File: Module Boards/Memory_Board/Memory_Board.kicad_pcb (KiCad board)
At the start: 6 copper layers, 10.8 x 15.2 mm, 17 parts, among them U1 MX25U12832FZNI02-TR, U2 MX25U25643GZ4I00-T

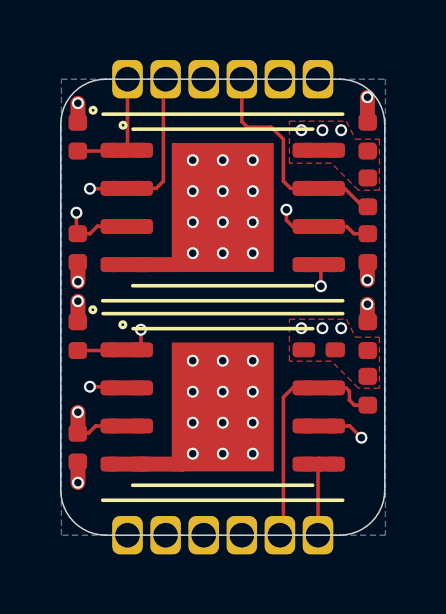
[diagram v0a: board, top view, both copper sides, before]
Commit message: Added Memory Socket Board. Improved layout of the Module Board
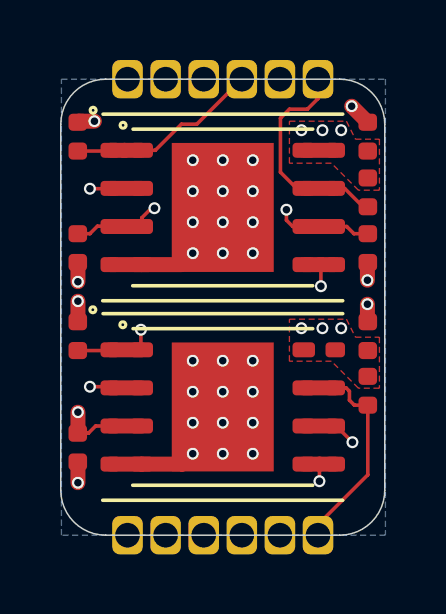
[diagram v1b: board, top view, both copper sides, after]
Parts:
- turned J1 to 90 degrees
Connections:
- J1 pad 10: ~{FLASH_1_WP}_(IO2) -> GND
- J1 pad 12: ~{FLASH_1_CS} -> FLASH_MOSI_(IO0)
- J1 pad 3: ~{FLASH_2_WP}_(IO2) -> FLASH_CLK
- J1 pad 5: ~{FLASH_2_RST}_(IO3) -> ~{FLASH_2_WP}_(IO2)
- J1 pad 6: FLASH_MOSI_(IO0) -> ~{FLASH_2_RST}_(IO3)
- J1 pad 7: FLASH_CLK -> ~{FLASH_1_RST}_(IO3)
- J1 pad 8: GND -> ~{FLASH_1_WP}_(IO2)
- J1 pad 9: ~{FLASH_1_RST}_(IO3) -> ~{FLASH_1_CS}
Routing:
- net ~{FLASH_2_WP}_(IO2): track 9.23 -> 18.8 mm
- net FLASH_MOSI_(IO0): track 15.3 -> 22.9 mm, vias 1 -> 2
- net ~{FLASH_1_CS}: track 4.56 -> 6.46 mm
- net FLASH_CLK: track 22.3 -> 24.1 mm
- net ~{FLASH_2_CS}: track 11.7 -> 12.2 mm
- net ~{FLASH_1_WP}_(IO2): track 10.1 -> 10.6 mm
